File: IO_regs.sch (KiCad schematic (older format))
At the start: 77 parts, among them U17 74HC04, U231 74HC245, U232 74HC04, U233 74HC04, U234 74LS373, U4 74HC04, U43 74HC04, U44 74HC04, U46 74HC04, U47 74HC04, U50 74HC04, U51 74HC04, U52 74HC04, U6 74HC04

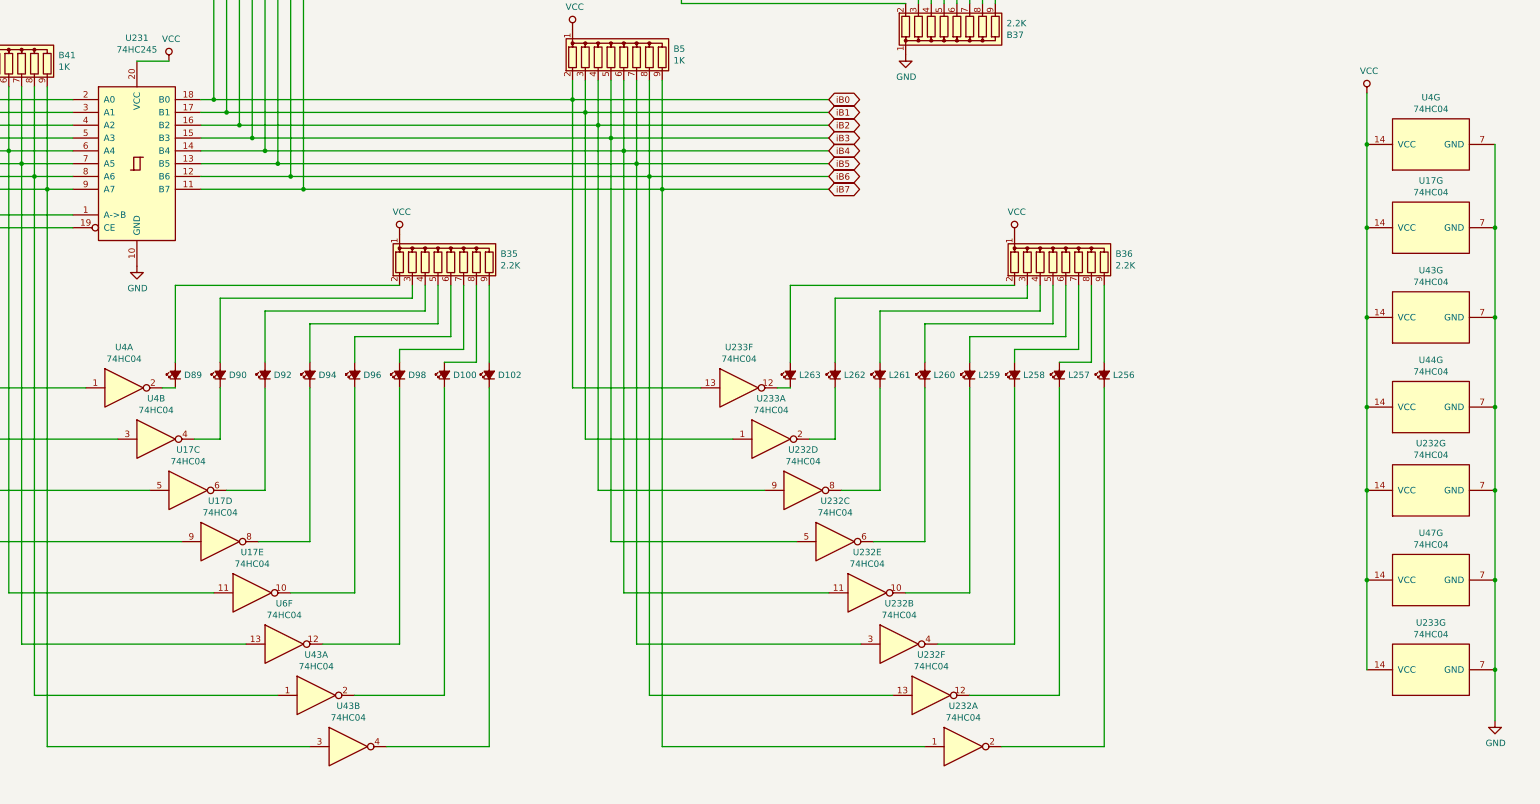
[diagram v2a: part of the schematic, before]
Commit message: place u229, u230 and D0-D7 leds
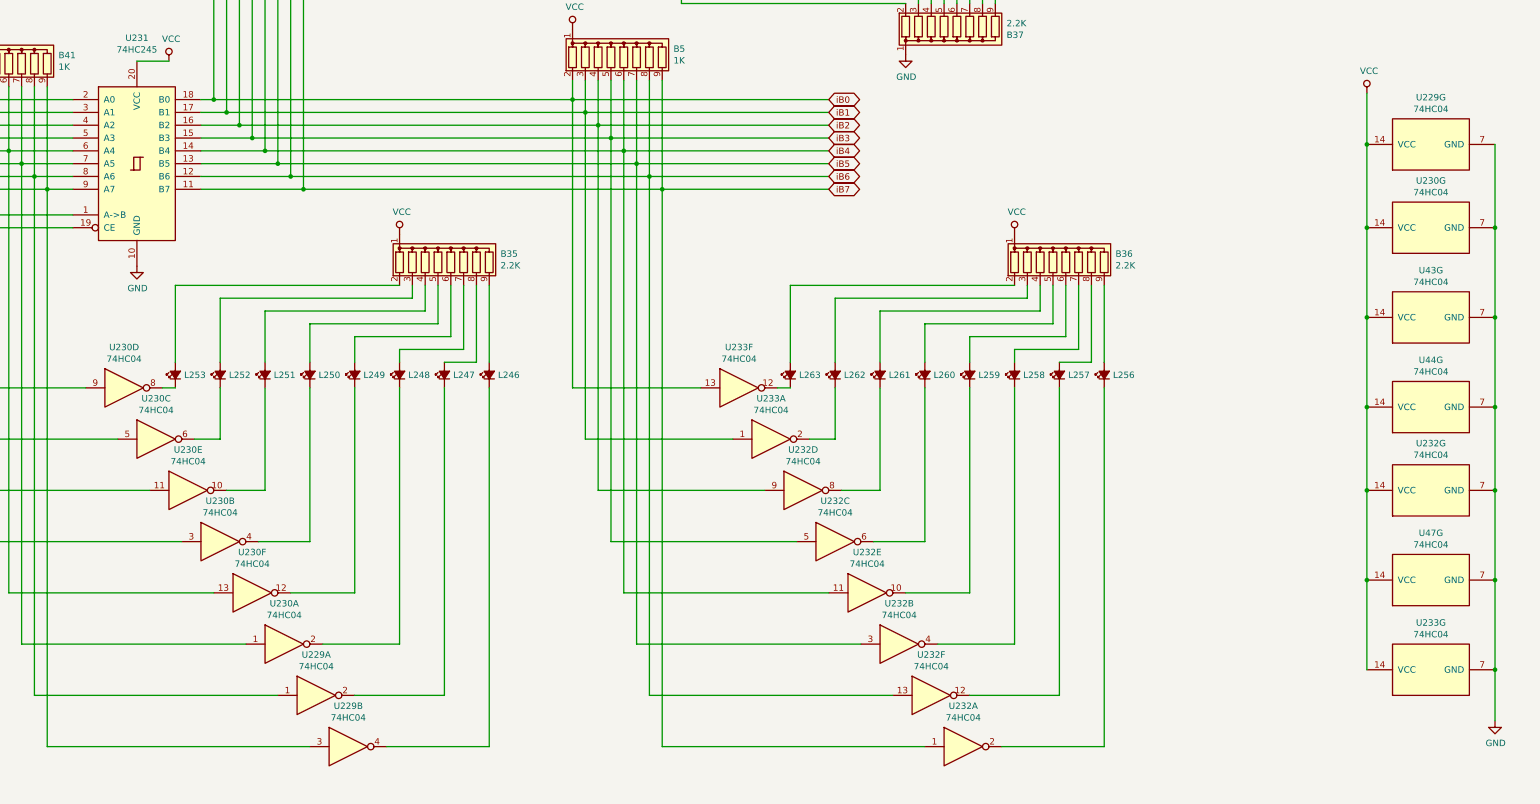
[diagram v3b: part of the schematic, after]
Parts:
- renumbered D102 to L246, D100 to L247, D98 to L248, D96 to L249, D94 to L250, D92 to L251, D90 to L252, D89 to L253, U43 to U229, U4 to U229, U4 to U230, U17 to U230, U6 to U230
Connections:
- net io_D0: now also U230.9; no longer U230.1
- net io_D1: now also U230.5; no longer U230.3
- net io_D2: now also U230.11; no longer U230.5
- net io_D3: now also U230.3; no longer U230.9
- net io_D4: now also U230.13; no longer U230.11
- net io_D5: now also U230.1; no longer U230.13
- net at L253.1 (K): now also U230.8; no longer U230.2
- net at L252.1 (K): now also U230.6; no longer U230.4
- net at L251.1 (K): now also U230.10; no longer U230.6
- net at L250.1 (K): now also U230.4; no longer U230.8
- net at L249.1 (K): now also U230.12; no longer U230.10
- net at L248.1 (K): now also U230.2; no longer U230.12
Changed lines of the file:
@@
 $EndComp
 $Comp
-L Device:LED_Small_ALT D89
+L Device:LED_Small_ALT L253
 U 1 1 5E3CD960
 P 2950 6100
-F 0 "D89" V 2950 6032 50  0000 R CNN
+F 0 "L253" V 2950 6032 50  0000 R CNN
 F 1 "LED_Small_ALT" V 2905 6032 50  0001 R CNN
 F 2 "LED_THT:LED_D3.0mm" V 2950 6100 50  0001 C CNN
@@
 $EndComp
 $Comp
-L Device:LED_Small_ALT D90
+L Device:LED_Small_ALT L252
 U 1 1 5E3D2330
 P 3300 6100
-F 0 "D90" V 3300 6032 50  0000 R CNN
+F 0 "L252" V 3300 6032 50  0000 R CNN
 F 1 "LED_Small_ALT" V 3255 6032 50  0001 R CNN
 F 2 "LED_THT:LED_D3.0mm" V 3300 6100 50  0001 C CNN
@@
 $EndComp
 $Comp
-L Device:LED_Small_ALT D92
+L Device:LED_Small_ALT L251
 U 1 1 5E3D687F
 P 3650 6100
-F 0 "D92" V 3650 6032 50  0000 R CNN
+F 0 "L251" V 3650 6032 50  0000 R CNN
 F 1 "LED_Small_ALT" V 3605 6032 50  0001 R CNN
 F 2 "LED_THT:LED_D3.0mm" V 3650 6100 50  0001 C CNN
@@
 $EndComp
 $Comp
-L Device:LED_Small_ALT D94
+L Device:LED_Small_ALT L250
 U 1 1 5E3D8E9F
 P 4000 6100
-F 0 "D94" V 4000 6032 50  0000 R CNN
+F 0 "L250" V 4000 6032 50  0000 R CNN
 F 1 "LED_Small_ALT" V 3955 6032 50  0001 R CNN
 F 2 "LED_THT:LED_D3.0mm" V 4000 6100 50  0001 C CNN
@@
 $EndComp
 $Comp
-L Device:LED_Small_ALT D96
+L Device:LED_Small_ALT L249
 U 1 1 5E3DB703
 P 4350 6100
-F 0 "D96" V 4350 6032 50  0000 R CNN
+F 0 "L249" V 4350 6032 50  0000 R CNN
 F 1 "LED_Small_ALT" V 4305 6032 50  0001 R CNN
 F 2 "LED_THT:LED_D3.0mm" V 4350 6100 50  0001 C CNN
@@
 $EndComp
 $Comp
-L Device:LED_Small_ALT D98
+L Device:LED_Small_ALT L248
 U 1 1 5E3DB709
 P 4700 6100
-F 0 "D98" V 4700 6032 50  0000 R CNN
+F 0 "L248" V 4700 6032 50  0000 R CNN
 F 1 "LED_Small_ALT" V 4655 6032 50  0001 R CNN
 F 2 "LED_THT:LED_D3.0mm" V 4700 6100 50  0001 C CNN
@@
 $EndComp
 $Comp
-L Device:LED_Small_ALT D100
+L Device:LED_Small_ALT L247
 U 1 1 5E3DB70F
 P 5050 6100
-F 0 "D100" V 5050 6032 50  0000 R CNN
+F 0 "L247" V 5050 6032 50  0000 R CNN
 F 1 "LED_Small_ALT" V 5005 6032 50  0001 R CNN
 F 2 "LED_THT:LED_D3.0mm" V 5050 6100 50  0001 C CNN
@@
 $EndComp
 $Comp
-L Device:LED_Small_ALT D102
+L Device:LED_Small_ALT L246
 U 1 1 5E3DB715
 P 5400 6100
-F 0 "D102" V 5400 6032 50  0000 R CNN
+F 0 "L246" V 5400 6032 50  0000 R CNN
 F 1 "LED_Small_ALT" V 5355 6032 50  0001 R CNN
 F 2 "LED_THT:LED_D3.0mm" V 5400 6100 50  0001 C CNN
@@
 Wire Wire Line
 	5400 5400 5400 6000
-$Comp
-L 74xx:74HC04 U4
-U 1 1 5E3F03E5
-P 2550 6200
-F 0 "U4" H 2550 6517 50  0000 C CNN
-F 1 "74HC04" H 2550 6426 50  0000 C CNN
-F 2 "Package_DIP:DIP-14_W7.62mm" H 2550 6200 50  0001 C CNN
-F 3 "https://assets.nexperia.com/documents/data-sheet/74HC_HCT04.pdf" H 2550 6200 50  0001 C CNN
-	1    2550 6200
-	1    0    0    -1
-$EndComp
-$Comp
-L 74xx:74HC04 U4
-U 2 1 5E3F15C1
-P 2800 6600
-F 0 "U4" H 2800 6917 50  0000 C CNN
-F 1 "74HC04" H 2800 6826 50  0000 C CNN
-F 2 "Package_DIP:DIP-14_W7.62mm" H 2800 6600 50  0001 C CNN
-F 3 "https://assets.nexperia.com/documents/data-sheet/74HC_HCT04.pdf" H 2800 6600 50  0001 C CNN
-	2    2800 6600
-	1    0    0    -1
-$EndComp
-$Comp
-L 74xx:74HC04 U17
-U 3 1 5E3F23FF
-P 3050 7000
-F 0 "U17" H 3050 7317 50  0000 C CNN
-F 1 "74HC04" H 3050 7226 50  0000 C CNN
-F 2 "Package_DIP:DIP-14_W7.62mm" H 3050 7000 50  0001 C CNN
-F 3 "https://assets.nexperia.com/documents/data-sheet/74HC_HCT04.pdf" H 3050 7000 50  0001 C CNN
-	3    3050 7000
-	1    0    0    -1
-$EndComp
-$Comp
-L 74xx:74HC04 U17
-U 4 1 5E3F4411
-P 3300 7400
-F 0 "U17" H 3300 7717 50  0000 C CNN
-F 1 "74HC04" H 3300 7626 50  0000 C CNN
-F 2 "Package_DIP:DIP-14_W7.62mm" H 3300 7400 50  0001 C CNN
-F 3 "https://assets.nexperia.com/documents/data-sheet/74HC_HCT04.pdf" H 3300 7400 50  0001 C CNN
-	4    3300 7400
-	1    0    0    -1
-$EndComp
-$Comp
-L 74xx:74HC04 U17
-U 5 1 5E3F508C
-P 3550 7800
-F 0 "U17" H 3550 8117 50  0000 C CNN
-F 1 "74HC04" H 3550 8026 50  0000 C CNN
-F 2 "Package_DIP:DIP-14_W7.62mm" H 3550 7800 50  0001 C CNN
-F 3 "https://assets.nexperia.com/documents/data-sheet/74HC_HCT04.pdf" H 3550 7800 50  0001 C CNN
-	5    3550 7800
-	1    0    0    -1
-$EndComp
-$Comp
-L 74xx:74HC04 U6
-U 6 1 5E3F5DEB
-P 3800 8200
-F 0 "U6" H 3800 8517 50  0000 C CNN
-F 1 "74HC04" H 3800 8426 50  0000 C CNN
-F 2 "Package_DIP:DIP-14_W7.62mm" H 3800 8200 50  0001 C CNN
-F 3 "https://assets.nexperia.com/documents/data-sheet/74HC_HCT04.pdf" H 3800 8200 50  0001 C CNN
-	6    3800 8200
-	1    0    0    -1
-$EndComp
 $Comp
 L 74xx:74HC04 U232
@@
 	7    12750 7000
 	0    -1   -1   0
-$EndComp
-$Comp
-L 74xx:74HC04 U43
-U 1 1 5E3FA84E
-P 4050 8600
-F 0 "U43" H 4050 8917 50  0000 C CNN
-F 1 "74HC04" H 4050 8826 50  0000 C CNN
-F 2 "Package_DIP:DIP-14_W7.62mm" H 4050 8600 50  0001 C CNN
-F 3 "https://assets.nexperia.com/documents/data-sheet/74HC_HCT04.pdf" H 4050 8600 50  0001 C CNN
-	1    4050 8600
-	1    0    0    -1
-$EndComp
-$Comp
-L 74xx:74HC04 U43
-U 2 1 5E3FB627
-P 4300 9000
-F 0 "U43" H 4300 9317 50  0000 C CNN
-F 1 "74HC04" H 4300 9226 50  0000 C CNN
-F 2 "Package_DIP:DIP-14_W7.62mm" H 4300 9000 50  0001 C CNN
-F 3 "https://assets.nexperia.com/documents/data-sheet/74HC_HCT04.pdf" H 4300 9000 50  0001 C CNN
-	2    4300 9000
-	1    0    0    -1
 $EndComp
 Wire Wire Line
@@
 o_A15
 $Comp
-L 74xx:74HC04 U17
+L 74xx:74HC04 U230
 U 7 1 5F8A37FB
 P 12750 4950
-F 0 "U17" V 13117 4950 50  0000 C CNN
+F 0 "U230" V 13117 4950 50  0000 C CNN
 F 1 "74HC04" V 13026 4950 50  0000 C CNN
 F 2 "Package_DIP:DIP-14_W7.62mm" H 12750 4950 50  0001 C CNN
@@
 $EndComp
 $Comp
-L 74xx:74HC04 U4
+L 74xx:74HC04 U229
 U 7 1 5F8D62D1
 P 12750 4300
-F 0 "U4" V 13117 4300 50  0000 C CNN
+F 0 "U229" V 13117 4300 50  0000 C CNN
 F 1 "74HC04" V 13026 4300 50  0000 C CNN
 F 2 "Package_DIP:DIP-14_W7.62mm" H 12750 4300 50  0001 C CNN
@@
 	1    0    0    -1
 $EndComp
+$Comp
+L 74xx:74HC04 U229
+U 2 1 5E3FB627
+P 4300 9000
+F 0 "U229" H 4300 9317 50  0000 C CNN
+F 1 "74HC04" H 4300 9226 50  0000 C CNN
+F 2 "Package_DIP:DIP-14_W7.62mm" H 4300 9000 50  0001 C CNN
+F 3 "https://assets.nexperia.com/documents/data-sheet/74HC_HCT04.pdf" H 4300 9000 50  0001 C CNN
+	2    4300 9000
+	1    0    0    -1
+$EndComp
+$Comp
+L 74xx:74HC04 U229
+U 1 1 5E3FA84E
+P 4050 8600
+F 0 "U229" H 4050 8917 50  0000 C CNN
+F 1 "74HC04" H 4050 8826 50  0000 C CNN
+F 2 "Package_DIP:DIP-14_W7.62mm" H 4050 8600 50  0001 C CNN
+F 3 "https://assets.nexperia.com/documents/data-sheet/74HC_HCT04.pdf" H 4050 8600 50  0001 C CNN
+	1    4050 8600
+	1    0    0    -1
+$EndComp
+$Comp
+L 74xx:74HC04 U230
+U 1 1 5E3F5DEB
+P 3800 8200
+F 0 "U230" H 3800 8517 50  0000 C CNN
+F 1 "74HC04" H 3800 8426 50  0000 C CNN
+F 2 "Package_DIP:DIP-14_W7.62mm" H 3800 8200 50  0001 C CNN
+F 3 "https://assets.nexperia.com/documents/data-sheet/74HC_HCT04.pdf" H 3800 8200 50  0001 C CNN
+	1    3800 8200
+	1    0    0    -1
+$EndComp
+$Comp
+L 74xx:74HC04 U230
+U 6 1 5E3F508C
+P 3550 7800
+F 0 "U230" H 3550 8117 50  0000 C CNN
+F 1 "74HC04" H 3550 8026 50  0000 C CNN
+F 2 "Package_DIP:DIP-14_W7.62mm" H 3550 7800 50  0001 C CNN
+F 3 "https://assets.nexperia.com/documents/data-sheet/74HC_HCT04.pdf" H 3550 7800 50  0001 C CNN
+	6    3550 7800
+	1    0    0    -1
+$EndComp
+$Comp
+L 74xx:74HC04 U230
+U 2 1 5E3F4411
+P 3300 7400
+F 0 "U230" H 3300 7717 50  0000 C CNN
+F 1 "74HC04" H 3300 7626 50  0000 C CNN
+F 2 "Package_DIP:DIP-14_W7.62mm" H 3300 7400 50  0001 C CNN
+F 3 "https://assets.nexperia.com/documents/data-sheet/74HC_HCT04.pdf" H 3300 7400 50  0001 C CNN
+	2    3300 7400
+	1    0    0    -1
+$EndComp
+$Comp
+L 74xx:74HC04 U230
+U 5 1 5E3F23FF
+P 3050 7000
+F 0 "U230" H 3050 7317 50  0000 C CNN
+F 1 "74HC04" H 3050 7226 50  0000 C CNN
+F 2 "Package_DIP:DIP-14_W7.62mm" H 3050 7000 50  0001 C CNN
+F 3 "https://assets.nexperia.com/documents/data-sheet/74HC_HCT04.pdf" H 3050 7000 50  0001 C CNN
+	5    3050 7000
+	1    0    0    -1
+$EndComp
+$Comp
+L 74xx:74HC04 U230
+U 3 1 5E3F15C1
+P 2800 6600
+F 0 "U230" H 2800 6917 50  0000 C CNN
+F 1 "74HC04" H 2800 6826 50  0000 C CNN
+F 2 "Package_DIP:DIP-14_W7.62mm" H 2800 6600 50  0001 C CNN
+F 3 "https://assets.nexperia.com/documents/data-sheet/74HC_HCT04.pdf" H 2800 6600 50  0001 C CNN
+	3    2800 6600
+	1    0    0    -1
+$EndComp
+$Comp
+L 74xx:74HC04 U230
+U 4 1 5E3F03E5
+P 2550 6200
+F 0 "U230" H 2550 6517 50  0000 C CNN
+F 1 "74HC04" H 2550 6426 50  0000 C CNN
+F 2 "Package_DIP:DIP-14_W7.62mm" H 2550 6200 50  0001 C CNN
+F 3 "https://assets.nexperia.com/documents/data-sheet/74HC_HCT04.pdf" H 2550 6200 50  0001 C CNN
+	4    2550 6200
+	1    0    0    -1
+$EndComp

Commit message: address display leds set and half routed
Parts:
- added unit 7 of U228
- B1: renamed from RN19; value R_Network08 -> 1K
- B3: renamed from RN20; value R_Network08 -> 1K
- B33: renamed from RN16; value R_Network08 -> 2.2K
- B34: renamed from RN14; value R_Network08 -> 2.2K
- B43: renamed from RN10; value R_Network08 -> 1K
- B44: renamed from RN12; value R_Network08 -> 1K
- renumbered D122 to L230, D119 to L231, D116 to L232, D113 to L233, D110 to L234, D108 to L235, D106 to L236, D105 to L237, D104 to L238, D103 to L239, D101 to L240, D99 to L241, D97 to L242, D95 to L243, D93 to L244, D91 to L245, U47 to U227, U44 to U227, U43 to U228, U44 to U228, U46 to U228, U17 to U229, U43 to U229
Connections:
- net A0: now also U229.11; no longer U229.1
- net A10: now also U227.9; no longer U227.5
- net A11: now also U227.5; no longer U227.9
- net A13: now also U227.3; no longer U227.13
- net A14: now also U227.13; no longer U227.1
- net A15: now also U227.1; no longer U227.3
- net A2: now also U229.13; no longer U229.5
- net A3: now also U229.1; no longer U229.9
- net A4: now also U228.9; no longer U228.11
- net A5: now also U228.5; no longer U228.13
- net A6: now also U228.11; no longer U228.1
- net A8: now also U228.13; no longer U228.1
- net A9: now also U228.1; no longer U228.3
- net GND: now also U228.7 (GND)
- net VCC: now also U228.14 (VCC)
- net io_D6: now also U229.9; no longer U229.1
- net io_D7: now also U229.5; no longer U229.3
- net at L247.1 (K): now also U229.8; no longer U229.2
- net at L246.1 (K): now also U229.6; no longer U229.4
- net at L245.1 (K): now also U229.10; no longer U229.2
- net at L243.1 (K): now also U229.12; no longer U229.6
- net at L242.1 (K): now also U229.2; no longer U229.8
- net at L241.1 (K): now also U228.8; no longer U228.10
- net at L240.1 (K): now also U228.6; no longer U228.12
- net at L239.1 (K): now also U228.10; no longer U228.2
- net at L237.1 (K): now also U228.12; no longer U228.2
- net at L236.1 (K): now also U228.2; no longer U228.4
- net at L235.1 (K): now also U227.8; no longer U227.6
- net at L234.1 (K): now also U227.6; no longer U227.8
- net at L232.1 (K): now also U227.4; no longer U227.12
- net at L231.1 (K): now also U227.12; no longer U227.2
- net at L230.1 (K): now also U227.2; no longer U227.4
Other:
- moved on the sheet: U227G, U230G, U232G, U233G, U43G, U44G

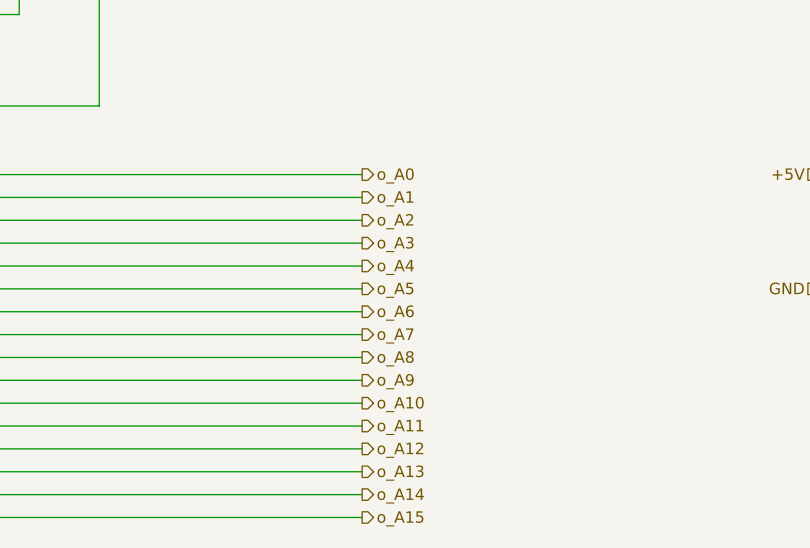
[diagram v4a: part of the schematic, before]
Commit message: placed WKL register, start routing
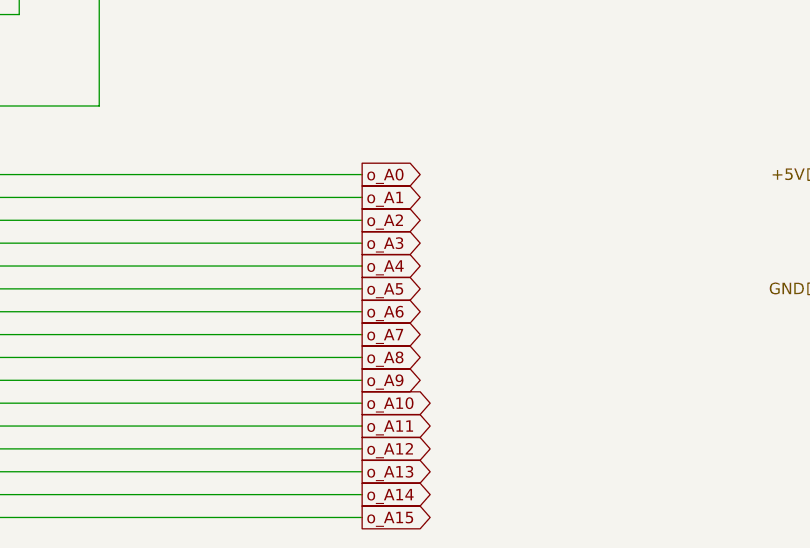
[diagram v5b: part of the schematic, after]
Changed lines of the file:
@@
 	1400 19000 10000 19000
 Connection ~ 1400 17200
-Text HLabel 10000 17500 2    50   Output ~ 0
-o_A0
-Text HLabel 10000 17600 2    50   Output ~ 0
-o_A1
-Text HLabel 10000 17700 2    50   Output ~ 0
-o_A2
-Text HLabel 10000 17800 2    50   Output ~ 0
-o_A3
-Text HLabel 10000 17900 2    50   Output ~ 0
-o_A4
-Text HLabel 10000 18000 2    50   Output ~ 0
-o_A5
-Text HLabel 10000 18100 2    50   Output ~ 0
-o_A6
-Text HLabel 10000 18200 2    50   Output ~ 0
-o_A7
-Text HLabel 10000 18300 2    50   Output ~ 0
-o_A8
-Text HLabel 10000 18400 2    50   Output ~ 0
-o_A9
-Text HLabel 10000 18500 2    50   Output ~ 0
-o_A10
-Text HLabel 10000 18600 2    50   Output ~ 0
-o_A11
-Text HLabel 10000 18700 2    50   Output ~ 0
-o_A12
-Text HLabel 10000 18800 2    50   Output ~ 0
-o_A13
-Text HLabel 10000 18900 2    50   Output ~ 0
-o_A14
-Text HLabel 10000 19000 2    50   Output ~ 0
-o_A15
 $Comp
 L 74xx:74HC04 U230
@@
 Wire Wire Line
 	12050 1950 12050 3000
+Text GLabel 10000 17500 2    50   Output ~ 0
+o_A0
+Text GLabel 10000 17600 2    50   Output ~ 0
+o_A1
+Text GLabel 10000 17700 2    50   Output ~ 0
+o_A2
+Text GLabel 10000 17800 2    50   Output ~ 0
+o_A3
+Text GLabel 10000 17900 2    50   Output ~ 0
+o_A4
+Text GLabel 10000 18000 2    50   Output ~ 0
+o_A5
+Text GLabel 10000 18100 2    50   Output ~ 0
+o_A6
+Text GLabel 10000 18200 2    50   Output ~ 0
+o_A7
+Text GLabel 10000 18300 2    50   Output ~ 0
+o_A8
+Text GLabel 10000 18400 2    50   Output ~ 0
+o_A9
+Text GLabel 10000 18500 2    50   Output ~ 0
+o_A10
+Text GLabel 10000 18600 2    50   Output ~ 0
+o_A11
+Text GLabel 10000 18700 2    50   Output ~ 0
+o_A12
+Text GLabel 10000 18800 2    50   Output ~ 0
+o_A13
+Text GLabel 10000 18900 2    50   Output ~ 0
+o_A14
+Text GLabel 10000 19000 2    50   Output ~ 0
+o_A15
 $EndSCHEMATC
